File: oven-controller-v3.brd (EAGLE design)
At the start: 57.4 x 82.7 mm, 48 parts, among them Q1 IRFL310, Q2 IRFL310, Q3 IRFL310, Q4 IRFL310, U1 ARDUINO_SHIELDLONGPADS, U2 MAX31855, U3 MAX31855, U4 MAX31855, U5 MAX31855, U6 MAX31855, U7 SN74LVC1G139

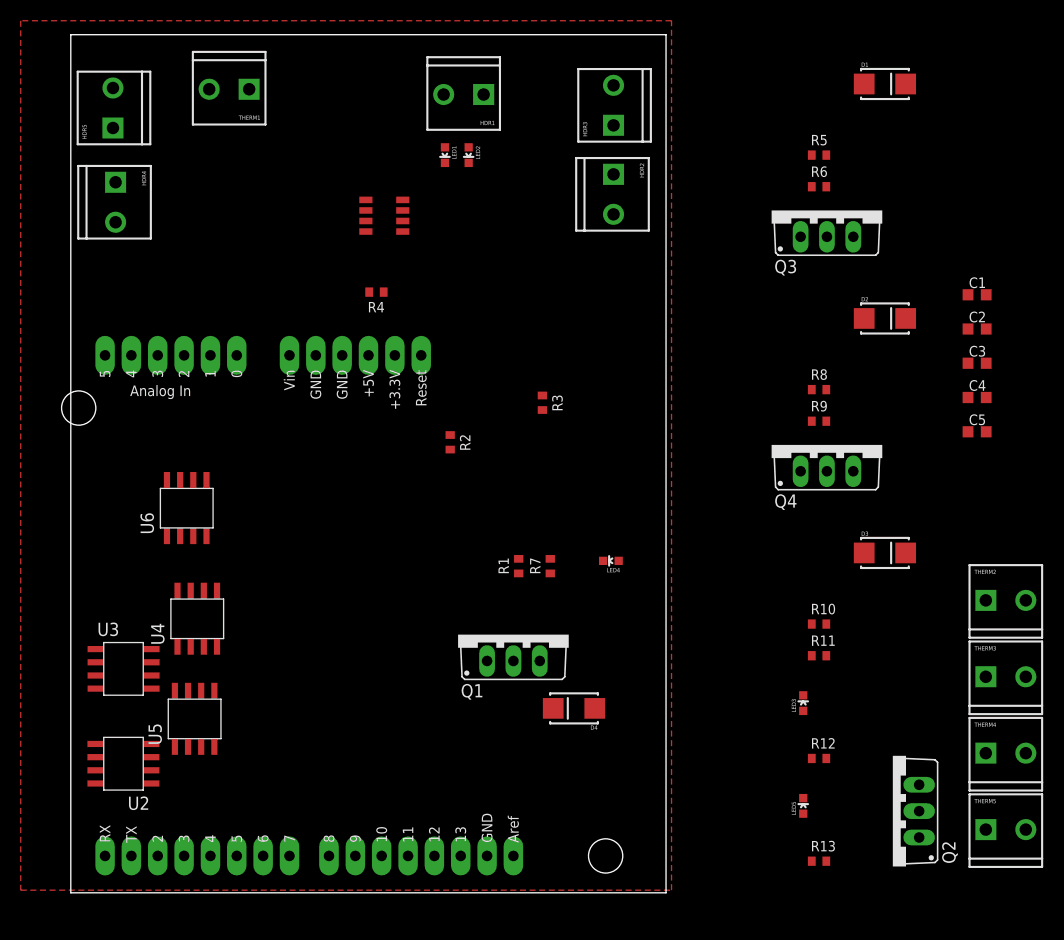
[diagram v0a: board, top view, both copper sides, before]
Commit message: Removed diodes. FETs now SOT23-3. Schematic and layout done. Ready for review.
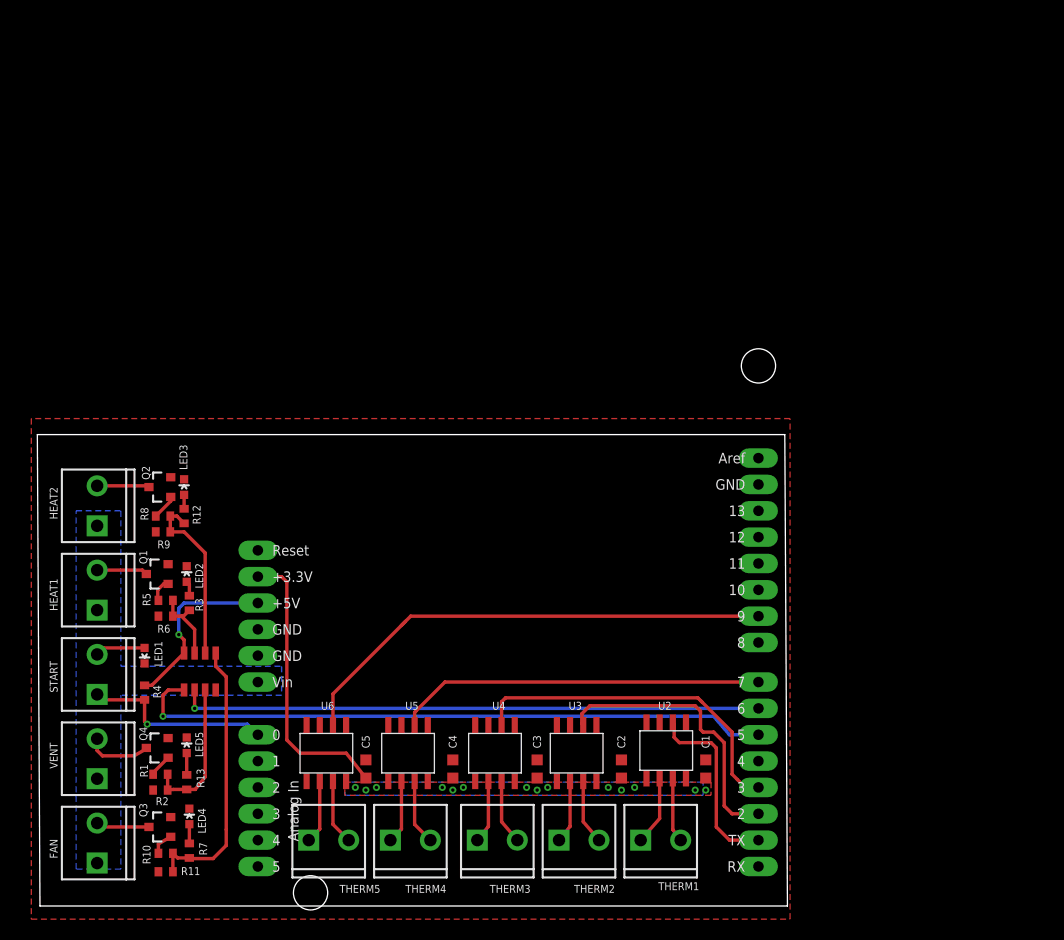
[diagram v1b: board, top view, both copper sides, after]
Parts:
- removed D1, D2, D3, D4: RS1DB-13-F, SparkFun-DiscreteSemi:SMA-DIODE_ALT
- removed HDR1: (no value), SparkFun-Connectors:SCREWTERMINAL-3.5MM-2_LOCK
- removed HDR2: HEAT1, SparkFun-Connectors:SCREWTERMINAL-3.5MM-2_LOCK
- removed HDR3: HEAT2, SparkFun-Connectors:SCREWTERMINAL-3.5MM-2_LOCK
- removed HDR4: FAN, SparkFun-Connectors:SCREWTERMINAL-3.5MM-2_LOCK
- removed HDR5: VENT, SparkFun-Connectors:SCREWTERMINAL-3.5MM-2_LOCK
- added FAN: HDR4, SparkFun-Connectors:SCREWTERMINAL-3.5MM-2_LOCK
- added HEAT1: HDR2, SparkFun-Connectors:SCREWTERMINAL-3.5MM-2_LOCK
- added HEAT2: HDR3, SparkFun-Connectors:SCREWTERMINAL-3.5MM-2_LOCK
- added START: HDR1, SparkFun-Connectors:SCREWTERMINAL-3.5MM-2_LOCK
- added VENT: HDR5, SparkFun-Connectors:SCREWTERMINAL-3.5MM-2_LOCK
- Q1, Q2, Q3, Q4: value IRFL310 -> FDV305N; device transistor-power:TO220BV -> SparkFun-DiscreteSemi:SOT23-3
- moved Q3 87.5 mm to (11.2, 6.35), turned to 90 degrees
- moved THERM1 81.8 mm to (57.7, 5.08), turned to 0 degrees
- moved Q2 77.2 mm to (11.2, 39.1)
- moved R5 76.2 mm to (11.7, 28.2)
- moved R6 75.4 mm to (11.7, 26.7)
- moved Q4 70.8 mm to (10.9, 14.0), turned to 90 degrees
- moved C5 67.3 mm to (31.0, 11.9), turned to 90 degrees
- moved R10 66.8 mm to (11.7, 3.81)
- moved R11 66.3 mm to (11.7, 2.03)
- moved R12 65.5 mm to (13.5, 36.3), turned to 270 degrees
- moved THERM5 65.3 mm to (25.7, 5.08)
- moved R8 64.4 mm to (11.4, 36.3)
- moved R9 64.1 mm to (11.4, 34.8)
- moved LED3 63.2 mm to (13.5, 39.1)
- moved C4 61.9 mm to (39.4, 11.9), turned to 90 degrees
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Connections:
- net 12V: now also FAN.1, HEAT1.1, HEAT2.1, VENT.1; no longer D1.C, D2.C, D3.C, D4.C, HDR2.1, HDR3.1, HDR4.1, HDR5.1
- net GND: now also Q1.2, Q2.2, Q3.2, Q4.2; no longer Q1.S, Q2.S, Q3.S, Q4.S
- net HDR3: now also FAN.2, Q3.3; no longer D3.A, HDR4.2, Q4.D
- net N$1: now also Q1.1; no longer Q2.G
- net N$10: now also START.2; no longer HDR1.2
- net N$2: now also Q4.1; no longer Q1.G
- net N$20: now also Q2.1; no longer Q3.G
- net N$21: now also HEAT2.2, Q2.3; no longer D2.A, HDR3.2, Q3.D
- net N$23: now also Q3.1; no longer Q4.G
- net N$3: now also Q4.3, VENT.2; no longer D4.A, HDR5.2, Q1.D
- net N$4: now also HEAT1.2, Q1.3; no longer D1.A, HDR2.2, Q2.D
- net START: now also START.1; no longer HDR1.1
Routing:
- net RELAY_MUX_SEL1: track 0.00 -> 62.5 mm, vias 0 -> 1
- net RELAY_MUX_SEL2: track 0.00 -> 56.1 mm, vias 0 -> 1
- net THERM_CS5: track 0.00 -> 47.7 mm
- net THERM_CS4: track 0.00 -> 35.6 mm
- net THERM_CS3: track 0.00 -> 33.3 mm
- net 3.3V: track 0.00 -> 27.6 mm, vias 0 -> 14
- net THERM_CS2: track 0.00 -> 27.4 mm
- net CS_FAN: track 0.00 -> 26.6 mm
- net START: track 0.00 -> 18.3 mm, vias 0 -> 1
- net THERM_CS1: track 0.00 -> 18.2 mm
- net 5V: track 0.00 -> 17.5 mm, vias 0 -> 1
- net CS_HEAT2: track 0.00 -> 17.0 mm
- net CS_VENT: track 0.00 -> 14.1 mm
- net CS_HEAT1: track 0.00 -> 7.43 mm
- net N$5: track 0.00 -> 6.63 mm
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- added copper zone on layer 16, net 12V
- added copper zone on layer 1, net 3.3V
- added copper zone on layer 16, net 3.3V
- added copper zone on layer 1, net GND
- removed copper zone on layer 1, net N$22
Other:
- board size 57.4 x 82.7 mm -> 72.3 x 45.4 mm
